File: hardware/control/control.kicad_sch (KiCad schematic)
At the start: 58 parts, among them J1 Conn_01x05_Male, J2 CANPWR, J3 CANGND, J4 RJ45, J5 RJ45, J6 Conn_02x03_Odd_Even, J7 DCDC-PWM, J8 DCDC-MEASURES, Q1 BSS123, SW1 next, SW2 select, U1 2.048V, U2 AP63200WU, U3 PIC18F27Q84, U4 TLE9250VSJXUMA1, Y1 10Mhz

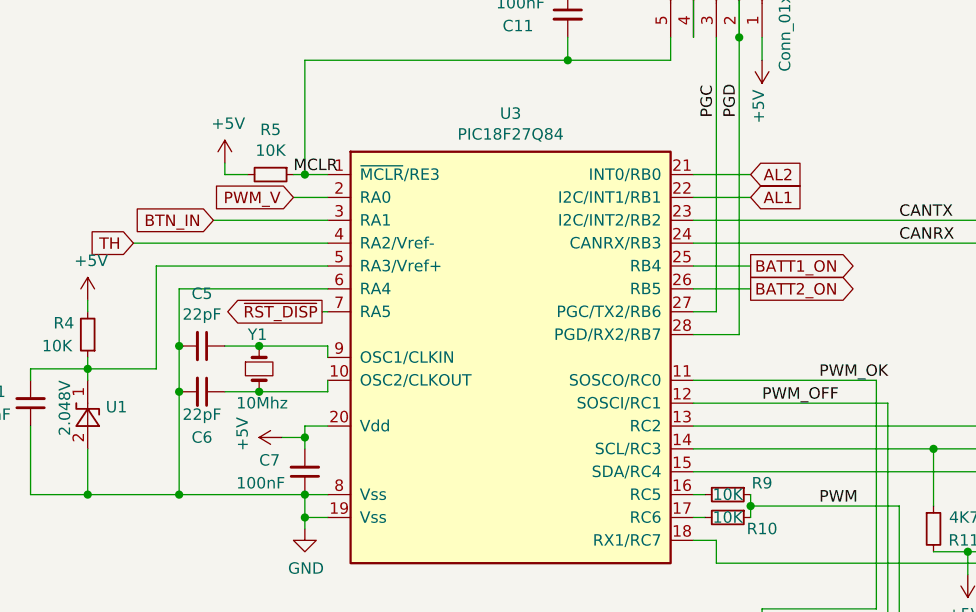
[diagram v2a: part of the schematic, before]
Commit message: Route control board. Will need a separate board for display.
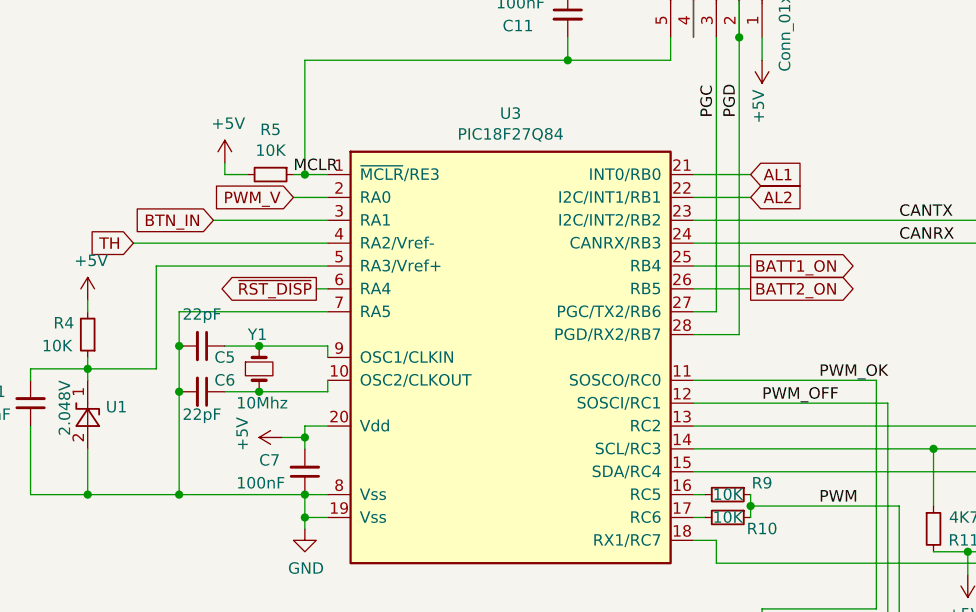
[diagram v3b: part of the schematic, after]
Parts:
- J1: footprint Connector_PinHeader_2.54mm:PinHeader_1x05_P2.54mm_Vertical -> Connector_PinHeader_2.54mm:PinHeader_1x05_P2.54mm_Horizontal
- J4, J5: footprint Connector_RJ:RJ45_Amphenol_54602-x08_Horizontal -> local:RJ45_Amphenol_54602-x08_Horizontal_handsolder
- R10, R11, R12, R9: footprint Resistor_SMD:R_0805_2012Metric_Pad1.20x1.40mm_HandSolder -> Resistor_THT:R_Axial_DIN0309_L9.0mm_D3.2mm_P12.70mm_Horizontal
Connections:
- net AL1: now also U3.21 (INT0/RB0); no longer U3.22 (I2C/INT1/RB1)
- net AL2: now also U3.22 (I2C/INT1/RB1); no longer U3.21 (INT0/RB0)
- net GND: now also U3.7 (RA5); no longer U3.6 (RA4)
- net ~{RST_DISP}: now also U3.6 (RA4); no longer U3.7 (RA5)
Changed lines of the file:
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@@
-    (stroke (width 0) (type default) (color 0 0 0 0))
-  )
-  (wire (pts (xy 44.45 62.23) (xy 60.96 62.23))
     (stroke (width 0) (type default) (color 0 0 0 0))
   )
@@
     (stroke (width 0) (type default) (color 0 0 0 0))
   )
+  (wire (pts (xy 59.69 62.23) (xy 60.96 62.23))
+    (stroke (width 0) (type default) (color 0 0 0 0))
+  )
   (wire (pts (xy 87.63 34.29) (xy 87.63 36.83))
     (stroke (width 0) (type default) (color 0 0 0 0))
@@
     (stroke (width 0) (type default) (color 0 0 0 0))
   )
-  (wire (pts (xy 60.325 64.77) (xy 60.96 64.77))
-    (stroke (width 0) (type default) (color 0 0 0 0))
-  )
   (wire (pts (xy 34.29 85.09) (xy 27.94 85.09))
     (stroke (width 0) (type default) (color 0 0 0 0))
@@
     (stroke (width 0) (type default) (color 0 0 0 0))
   )
-  (wire (pts (xy 44.45 62.23) (xy 44.45 68.58))
-    (stroke (width 0) (type default) (color 0 0 0 0))
-  )
   (wire (pts (xy 44.45 85.09) (xy 58.42 85.09))
     (stroke (width 0) (type default) (color 0 0 0 0))
@@
     (stroke (width 0) (type default) (color 0 0 0 0))
   )
+  (wire (pts (xy 44.45 64.77) (xy 44.45 68.58))
+    (stroke (width 0) (type default) (color 0 0 0 0))
+  )
   (wire (pts (xy 144.78 46.99) (xy 144.78 49.53))
     (stroke (width 0) (type default) (color 0 0 0 0))
@@
   )
   (wire (pts (xy 179.07 92.71) (xy 179.07 91.44))
+    (stroke (width 0) (type default) (color 0 0 0 0))
+  )
+  (wire (pts (xy 44.45 64.77) (xy 60.96 64.77))
     (stroke (width 0) (type default) (color 0 0 0 0))
   )
@@
     )
   )
-  (global_label "AL2" (shape input) (at 107.95 49.53 0) (fields_autoplaced)
+  (global_label "AL2" (shape input) (at 107.95 52.07 0) (fields_autoplaced)
     (effects (font (size 1.27 1.27)) (justify left))
-    (property "Intersheet References" "${INTERSHEET_REFS}" (id 0) (at 113.6893 49.4506 0)
+    (property "Intersheet References" "${INTERSHEET_REFS}" (id 0) (at 113.6893 51.9906 0)
       (effects (font (size 1.27 1.27)) (justify left) hide)
     )
@@
     )
   )
-  (global_label "AL1" (shape input) (at 107.95 52.07 0) (fields_autoplaced)
+  (global_label "AL1" (shape input) (at 107.95 49.53 0) (fields_autoplaced)
     (effects (font (size 1.27 1.27)) (justify left))
-    (property "Intersheet References" "${INTERSHEET_REFS}" (id 0) (at 113.6893 51.9906 0)
+    (property "Intersheet References" "${INTERSHEET_REFS}" (id 0) (at 113.6893 49.4506 0)
       (effects (font (size 1.27 1.27)) (justify left) hide)
     )
@@
     )
   )
-  (global_label "~{RST_DISP}" (shape output) (at 60.325 64.77 180) (fields_autoplaced)
+  (global_label "~{RST_DISP}" (shape output) (at 59.69 62.23 180) (fields_autoplaced)
     (effects (font (size 1.27 1.27)) (justify right))
-    (property "Intersheet References" "${INTERSHEET_REFS}" (id 0) (at 49.1429 64.8494 0)
+    (property "Intersheet References" "${INTERSHEET_REFS}" (id 0) (at 48.5079 62.3094 0)
       (effects (font (size 1.27 1.27)) (justify right) hide)
     )
@@
       (effects (font (size 1.27 1.27)) (justify right))
     )
-    (property "Footprint" "Resistor_SMD:R_0805_2012Metric_Pad1.20x1.40mm_HandSolder" (id 2) (at 128.27 88.9 0)
+    (property "Footprint" "Resistor_THT:R_Axial_DIN0309_L9.0mm_D3.2mm_P12.70mm_Horizontal" (id 2) (at 128.27 88.9 0)
       (effects (font (size 1.27 1.27)) hide)
     )
@@
       (effects (font (size 1.27 1.27)) (justify right))
     )
-    (property "Footprint" "Connector_PinHeader_2.54mm:PinHeader_1x05_P2.54mm_Vertical" (id 2) (at 104.14 29.21 0)
+    (property "Footprint" "Connector_PinHeader_2.54mm:PinHeader_1x05_P2.54mm_Horizontal" (id 2) (at 104.14 29.21 0)
       (effects (font (size 1.27 1.27)) hide)
     )
@@
       (effects (font (size 1.27 1.27)) (justify right))
     )
-    (property "Footprint" "Connector_RJ:RJ45_Amphenol_54602-x08_Horizontal" (id 2) (at 241.3 53.975 90)
+    (property "Footprint" "local:RJ45_Amphenol_54602-x08_Horizontal_handsolder" (id 2) (at 241.3 53.975 90)
       (effects (font (size 1.27 1.27)) hide)
     )
@@
       (effects (font (size 1.27 1.27)) (justify right))
     )
-    (property "Footprint" "Connector_RJ:RJ45_Amphenol_54602-x08_Horizontal" (id 2) (at 217.17 53.975 90)
+    (property "Footprint" "local:RJ45_Amphenol_54602-x08_Horizontal_handsolder" (id 2) (at 217.17 53.975 90)
       (effects (font (size 1.27 1.27)) hide)
     )
@@
   (symbol (lib_id "Device:C_Small") (at 46.99 73.66 270) (unit 1)
     (in_bom yes) (on_board yes)
-    (property "Reference" "C6" (id 0) (at 46.99 78.74 90))
+    (property "Reference" "C6" (id 0) (at 49.53 72.39 90))
     (property "Value" "22pF" (id 1) (at 46.99 76.2 90))
     (property "Footprint" "Capacitor_THT:C_Disc_D3.8mm_W2.6mm_P2.50mm" (id 2) (at 46.99 73.66 0)
@@
       (effects (font (size 1.27 1.27)) (justify right))
     )
-    (property "Footprint" "Resistor_SMD:R_0805_2012Metric_Pad1.20x1.40mm_HandSolder" (id 2) (at 134.62 88.9 0)
+    (property "Footprint" "Resistor_THT:R_Axial_DIN0309_L9.0mm_D3.2mm_P12.70mm_Horizontal" (id 2) (at 134.62 88.9 0)
       (effects (font (size 1.27 1.27)) hide)
     )
@@
   (symbol (lib_id "Device:C_Small") (at 46.99 68.58 270) (unit 1)
     (in_bom yes) (on_board yes)
-    (property "Reference" "C5" (id 0) (at 46.99 62.7634 90))
+    (property "Reference" "C5" (id 0) (at 49.53 69.85 90))
     (property "Value" "22pF" (id 1) (at 46.99 65.0748 90))
     (property "Footprint" "Capacitor_THT:C_Disc_D3.8mm_W2.6mm_P2.50mm" (id 2) (at 46.99 68.58 0)
@@
     (property "Reference" "R10" (id 0) (at 109.22 88.9 90))
     (property "Value" "10K" (id 1) (at 105.41 87.63 90))
-    (property "Footprint" "Resistor_SMD:R_0805_2012Metric_Pad1.20x1.40mm_HandSolder" (id 2) (at 105.41 87.63 0)
+    (property "Footprint" "Resistor_THT:R_Axial_DIN0309_L9.0mm_D3.2mm_P12.70mm_Horizontal" (id 2) (at 105.41 87.63 0)
       (effects (font (size 1.27 1.27)) hide)
     )
@@
     (property "Reference" "R9" (id 0) (at 109.22 83.82 90))
     (property "Value" "10K" (id 1) (at 105.41 85.09 90))
-    (property "Footprint" "Resistor_SMD:R_0805_2012Metric_Pad1.20x1.40mm_HandSolder" (id 2) (at 105.41 85.09 0)
+    (property "Footprint" "Resistor_THT:R_Axial_DIN0309_L9.0mm_D3.2mm_P12.70mm_Horizontal" (id 2) (at 105.41 85.09 0)
       (effects (font (size 1.27 1.27)) hide)
     )
@@
     )
     (path "/2f9ee5b6-ea05-4a48-b884-75b3a992d209"
-      (reference "J1") (unit 1) (value "Conn_01x05_Male") (footprint "Connector_PinHeader_2.54mm:PinHeader_1x05_P2.54mm_Vertical")
+      (reference "J1") (unit 1) (value "Conn_01x05_Male") (footprint "Connector_PinHeader_2.54mm:PinHeader_1x05_P2.54mm_Horizontal")
     )
     (path "/6faf117b-b455-40c2-98d8-3372c7f176c2"
@@
     )
     (path "/385cdd38-5495-4d4e-ba24-99aa11999e7c"
-      (reference "J4") (unit 1) (value "RJ45") (footprint "Connector_RJ:RJ45_Amphenol_54602-x08_Horizontal")
+      (reference "J4") (unit 1) (value "RJ45") (footprint "local:RJ45_Amphenol_54602-x08_Horizontal_handsolder")
     )
     (path "/33b6052e-24c7-4c69-8307-d7c4c128421c"
-      (reference "J5") (unit 1) (value "RJ45") (footprint "Connector_RJ:RJ45_Amphenol_54602-x08_Horizontal")
+      (reference "J5") (unit 1) (value "RJ45") (footprint "local:RJ45_Amphenol_54602-x08_Horizontal_handsolder")
     )
     (path "/55b20b44-a1ee-4f56-9493-46f4583deb01"
@@
     )
     (path "/d4cced01-c3b2-457e-9630-ede399fc8c31"
-      (reference "R9") (unit 1) (value "10K") (footprint "Resistor_SMD:R_0805_2012Metric_Pad1.20x1.40mm_HandSolder")
+      (reference "R9") (unit 1) (value "10K") (footprint "Resistor_THT:R_Axial_DIN0309_L9.0mm_D3.2mm_P12.70mm_Horizontal")
     )
     (path "/c828a5e3-fc2a-4595-959c-e2638d431d51"
-      (reference "R10") (unit 1) (value "10K") (footprint "Resistor_SMD:R_0805_2012Metric_Pad1.20x1.40mm_HandSolder")
+      (reference "R10") (unit 1) (value "10K") (footprint "Resistor_THT:R_Axial_DIN0309_L9.0mm_D3.2mm_P12.70mm_Horizontal")
     )
     (path "/0b89861b-d684-4581-aab7-bfb40d7ac71f"
-      (reference "R11") (unit 1) (value "4K7") (footprint "Resistor_SMD:R_0805_2012Metric_Pad1.20x1.40mm_HandSolder")
+      (reference "R11") (unit 1) (value "4K7") (footprint "Resistor_THT:R_Axial_DIN0309_L9.0mm_D3.2mm_P12.70mm_Horizontal")
     )
     (path "/51f0f55e-83ce-4497-b09e-c6e1e4b03e19"
-      (reference "R12") (unit 1) (value "4K7") (footprint "Resistor_SMD:R_0805_2012Metric_Pad1.20x1.40mm_HandSolder")
+      (reference "R12") (unit 1) (value "4K7") (footprint "Resistor_THT:R_Axial_DIN0309_L9.0mm_D3.2mm_P12.70mm_Horizontal")
     )
     (path "/9cd13088-9280-42ff-88e7-8341e2a75837"

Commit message: Re-route PCBs to move RJ45 connectors on bottom, saving a bit of stack size.
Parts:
- J7, J8: P/N (none) -> DW-05-15-T-D-250
- R11: footprint Resistor_THT:R_Axial_DIN0309_L9.0mm_D3.2mm_P12.70mm_Horizontal -> Resistor_SMD:R_0805_2012Metric_Pad1.20x1.40mm_HandSolder
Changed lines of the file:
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@@
       (effects (font (size 1.27 1.27)) (justify right))
     )
-    (property "Footprint" "Resistor_THT:R_Axial_DIN0309_L9.0mm_D3.2mm_P12.70mm_Horizontal" (id 2) (at 128.27 88.9 0)
+    (property "Footprint" "Resistor_SMD:R_0805_2012Metric_Pad1.20x1.40mm_HandSolder" (id 2) (at 128.27 88.9 0)
       (effects (font (size 1.27 1.27)) hide)
     )
@@
       (effects (font (size 1.27 1.27)) hide)
     )
+    (property "P/N" "DW-05-15-T-D-250" (id 4) (at 114.3 110.49 0)
+      (effects (font (size 1.27 1.27)) hide)
+    )
     (pin "1")
     (pin "10")
@@
     )
     (property "Datasheet" "~" (id 3) (at 153.67 105.41 0)
+      (effects (font (size 1.27 1.27)) hide)
+    )
+    (property "P/N" "DW-05-15-T-D-250" (id 4) (at 153.67 105.41 0)
       (effects (font (size 1.27 1.27)) hide)
     )
@@
     )
     (path "/0b89861b-d684-4581-aab7-bfb40d7ac71f"
-      (reference "R11") (unit 1) (value "4K7") (footprint "Resistor_THT:R_Axial_DIN0309_L9.0mm_D3.2mm_P12.70mm_Horizontal")
+      (reference "R11") (unit 1) (value "4K7") (footprint "Resistor_SMD:R_0805_2012Metric_Pad1.20x1.40mm_HandSolder")
     )
     (path "/51f0f55e-83ce-4497-b09e-c6e1e4b03e19"

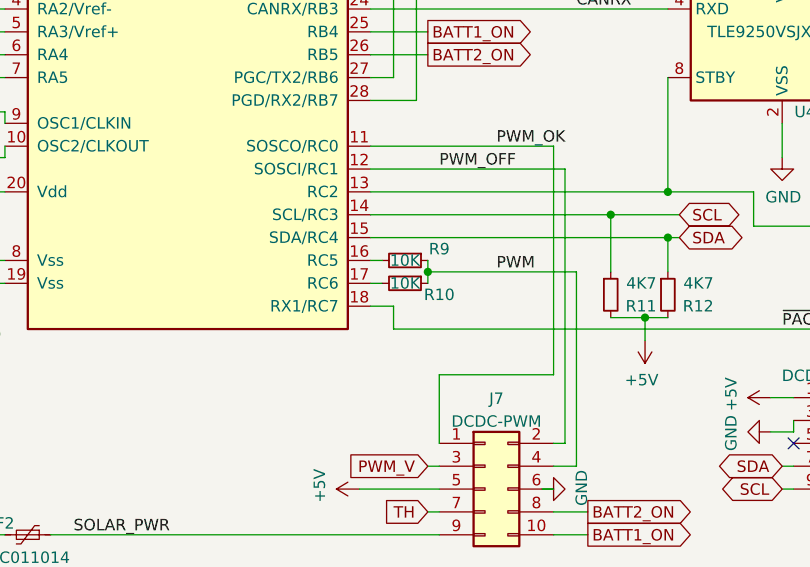
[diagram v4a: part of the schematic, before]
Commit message: Adjust PWM resistor divider to better match NCP5091B mid-state input voltage.
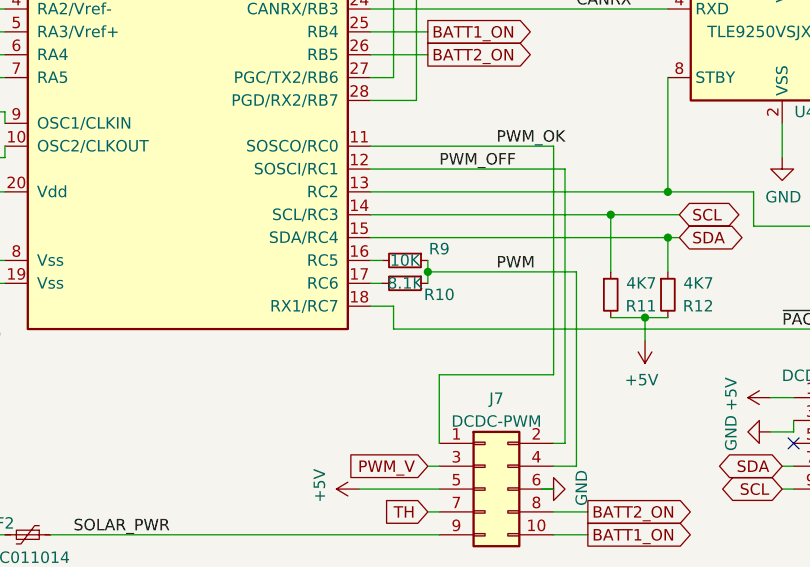
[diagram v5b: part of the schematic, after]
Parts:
- R10: value 10K -> 8.1K
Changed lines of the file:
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@@
     (in_bom yes) (on_board yes)
     (property "Reference" "R10" (id 0) (at 109.22 88.9 90))
-    (property "Value" "10K" (id 1) (at 105.41 87.63 90))
+    (property "Value" "8.1K" (id 1) (at 105.41 87.63 90))
     (property "Footprint" "Resistor_THT:R_Axial_DIN0309_L9.0mm_D3.2mm_P12.70mm_Horizontal" (id 2) (at 105.41 87.63 0)
       (effects (font (size 1.27 1.27)) hide)
@@
     )
     (path "/c828a5e3-fc2a-4595-959c-e2638d431d51"
-      (reference "R10") (unit 1) (value "10K") (footprint "Resistor_THT:R_Axial_DIN0309_L9.0mm_D3.2mm_P12.70mm_Horizontal")
+      (reference "R10") (unit 1) (value "8.1K") (footprint "Resistor_THT:R_Axial_DIN0309_L9.0mm_D3.2mm_P12.70mm_Horizontal")
     )
     (path "/0b89861b-d684-4581-aab7-bfb40d7ac71f"

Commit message: WIP on diaplay PCB.
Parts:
- removed DI1: MCOB128064JX, LCDdisplays.mod:MCOB128064JX, symbol LCDdisplays:MCOB128064JX
- added J9: display, Connector_Harwin:Harwin_M20-7810345_2x03_P2.54mm_Vertical, symbol Connector_Generic:Conn_02x03_Top_Bottom
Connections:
- net +5V: now also J9.1 (Pin_1)
- net GND: now also J9.3 (Pin_3)
- net SCL: now also J9.6 (Pin_6)
- net SDA: now also J9.5 (Pin_5)
- net ~{RST_DISP}: now also J9.4 (Pin_4)

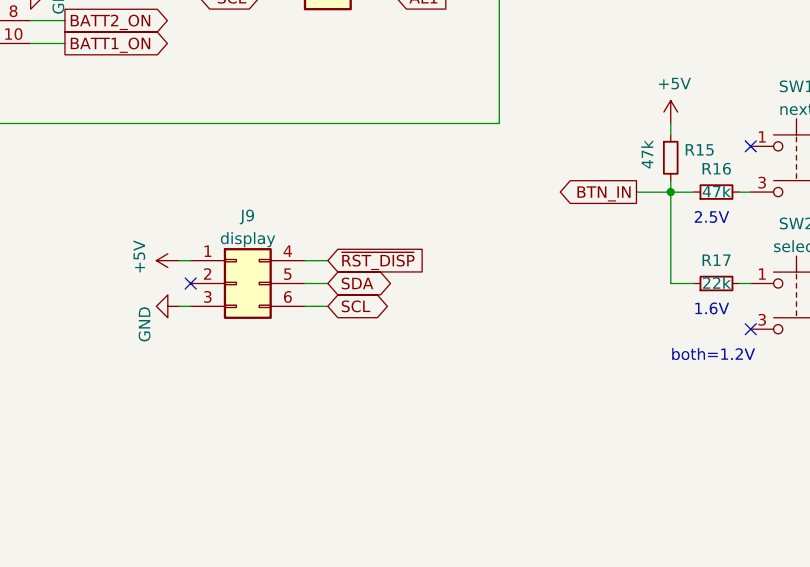
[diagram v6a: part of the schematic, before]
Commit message: Route display PCB. Adjust control for connector wiring changes.
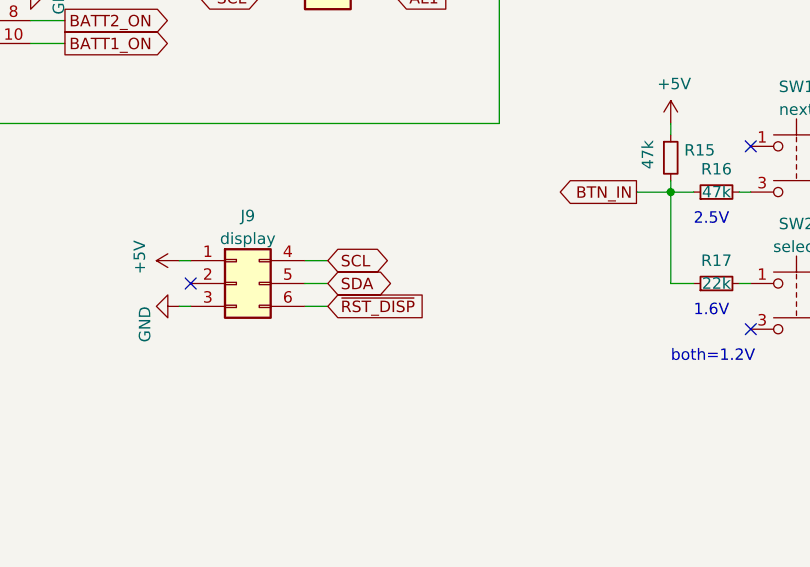
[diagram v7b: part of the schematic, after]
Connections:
- net SCL: now also J9.4 (Pin_4); no longer J9.6 (Pin_6)
- net ~{RST_DISP}: now also J9.6 (Pin_6); no longer J9.4 (Pin_4)
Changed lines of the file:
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@@
     )
   )
-  (global_label "SCL" (shape bidirectional) (at 154.94 144.78 0) (fields_autoplaced)
+  (global_label "SCL" (shape bidirectional) (at 154.94 139.7 0) (fields_autoplaced)
     (effects (font (size 1.27 1.27)) (justify left))
-    (property "Intersheet References" "${INTERSHEET_REFS}" (id 0) (at 160.8607 144.8594 0)
+    (property "Intersheet References" "${INTERSHEET_REFS}" (id 0) (at 160.8607 139.7794 0)
       (effects (font (size 1.27 1.27)) (justify left) hide)
     )
@@
     )
   )
-  (global_label "~{RST_DISP}" (shape input) (at 154.94 139.7 0) (fields_autoplaced)
+  (global_label "~{RST_DISP}" (shape input) (at 154.94 144.78 0) (fields_autoplaced)
     (effects (font (size 1.27 1.27)) (justify left))
-    (property "Intersheet References" "${INTERSHEET_REFS}" (id 0) (at 166.1221 139.7794 0)
+    (property "Intersheet References" "${INTERSHEET_REFS}" (id 0) (at 166.1221 144.8594 0)
       (effects (font (size 1.27 1.27)) (justify left) hide)
     )

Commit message: normalise and update P/N, update footprint to match
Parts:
- C1, C11, C13, C7: footprint Capacitor_SMD:C_0805_2012Metric_Pad1.18x1.45mm_HandSolder -> Capacitor_SMD:C_0603_1608Metric_Pad1.08x0.95mm_HandSolder; P/N (none) -> MC0603B104K250CT
- C4, C8: footprint Capacitor_SMD:C_0805_2012Metric_Pad1.18x1.45mm_HandSolder -> Capacitor_SMD:C_1206_3216Metric_Pad1.33x1.80mm_HandSolder; P/N CL21B104KBCNNWC -> C1206C104K5RACTU
- D1, D2: P/N PMEG4005EGWX -> PMEG4005EGWX (stock)
- J1, J6, R11, R12, R13, R15, R16, R4, R5, R8, R9, U3, U4, Y1: P/N (none) -> stock
- J4, J5: P/N 54601-908WPLF -> 54601-908WPLF (stock)
- R17: value 22k -> 22k
- R18: P/N MCWF08P1000FTL -> MCWF08P1000FTL (stock)
- U1: P/N LM4040DBZ-2.0 -> LM4040DBZ-2.0 (stock)
